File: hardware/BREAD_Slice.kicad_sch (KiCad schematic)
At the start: 0 parts

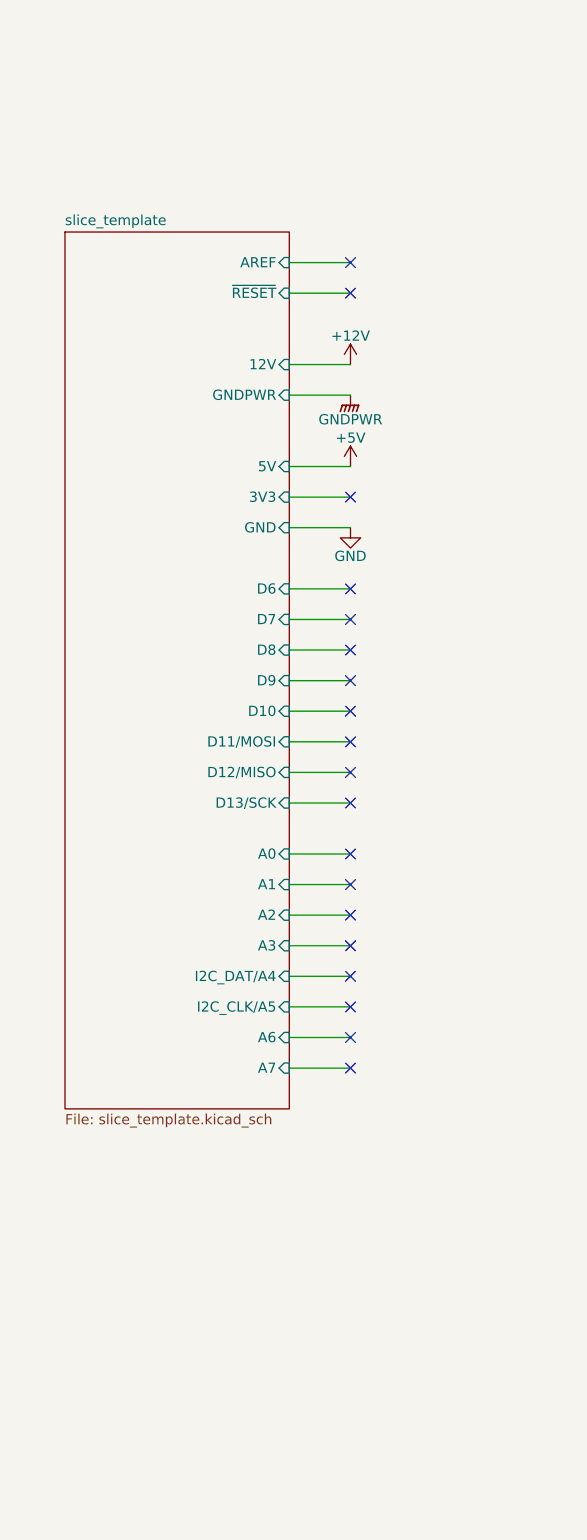
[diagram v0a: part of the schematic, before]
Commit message: Changed to Pico from nano
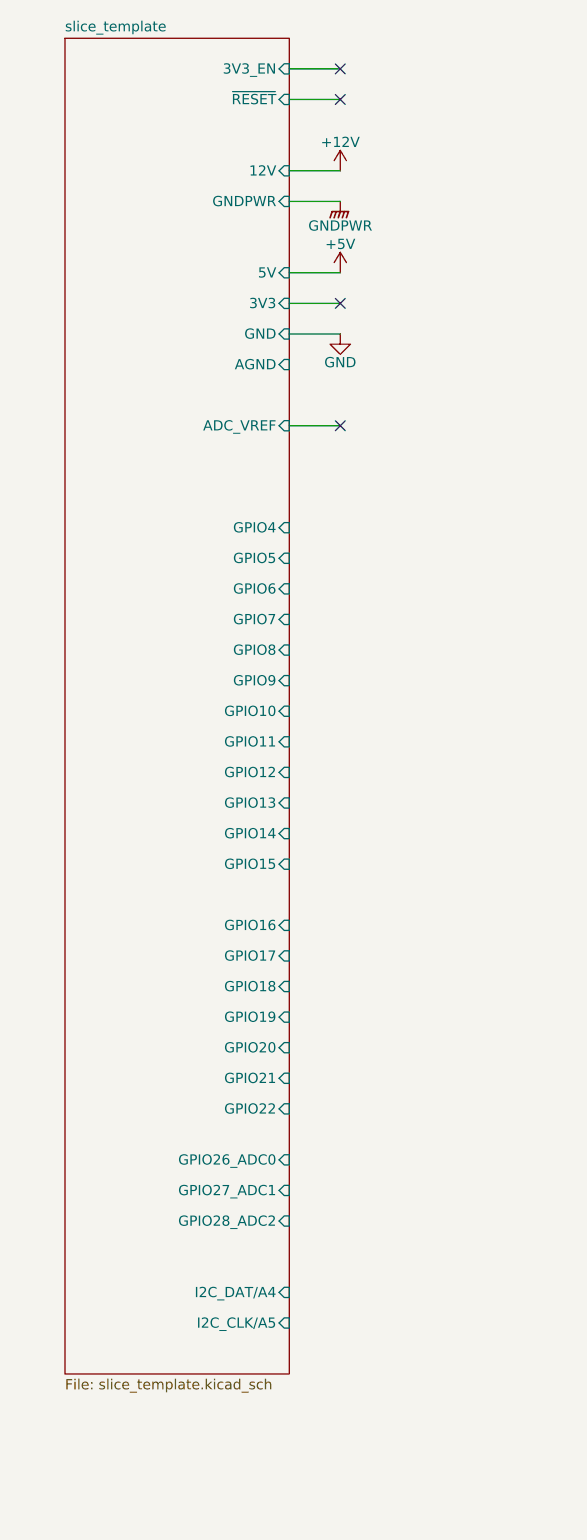
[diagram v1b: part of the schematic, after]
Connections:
- no-connect marks 19 -> 4
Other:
- sheet slice_template ports: added 3V3_EN, ADC_VREF, AGND, GPIO10, GPIO11, GPIO12, GPIO13, GPIO14, GPIO15, GPIO16, GPIO17, GPIO18, GPIO19, GPIO20, GPIO21, GPIO22, GPIO26_ADC0, GPIO27_ADC1, GPIO28_ADC2, GPIO4, GPIO5, GPIO6, GPIO7, GPIO8, GPIO9; removed A0, A1, A2, A3, A6, A7, AREF, D10, D11/MOSI, D12/MISO, D13/SCK, D6, D7, D8, D9

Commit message: added i2c and spi
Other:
- sheet slice_template ports: added I2C_CLK/GPIO7, I2C_SDA/GPIO6, SPI0_MISO/GPIO16, SPI0_MOSI/GPIO19, SPI0_SCK/GPIO18, SPI0_~{CS}/GPIO17; removed GPIO16, GPIO17, GPIO18, GPIO19, GPIO6, GPIO7, I2C_CLK/A5, I2C_DAT/A4
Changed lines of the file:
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@@
-			)
-		)
-		(pin "I2C_CLK{slash}A5" input
-			(at 45.72 177.8 0)
-			(effects
-				(font
-					(size 1.27 1.27)
-				)
-				(justify right)
-			)
-		)
-		(pin "I2C_DAT{slash}A4" input
-			(at 45.72 173.99 0)
-			(effects
-				(font
-					(size 1.27 1.27)
-				)
-				(justify right)
 			)
 		)
@@
 			)
 		)
-		(pin "GPIO6" input
-			(at 45.72 86.36 0)
-			(effects
-				(font
-					(size 1.27 1.27)
-				)
-				(justify right)
-			)
-		)
-		(pin "GPIO7" input
-			(at 45.72 90.17 0)
-			(effects
-				(font
-					(size 1.27 1.27)
-				)
-				(justify right)
-			)
-		)
 		(pin "GPIO8" input
 			(at 45.72 93.98 0)
@@
 			)
 		)
-		(pin "GPIO16" input
-			(at 45.72 128.27 0)
-			(effects
-				(font
-					(size 1.27 1.27)
-				)
-				(justify right)
-			)
-		)
 		(pin "AGND" input
 			(at 45.72 58.42 0)
@@
 			)
 		)
-		(pin "GPIO17" input
-			(at 45.72 132.08 0)
-			(effects
-				(font
-					(size 1.27 1.27)
-				)
-				(justify right)
-			)
-		)
-		(pin "GPIO18" input
-			(at 45.72 135.89 0)
-			(effects
-				(font
-					(size 1.27 1.27)
-				)
-				(justify right)
-			)
-		)
-		(pin "GPIO19" input
-			(at 45.72 139.7 0)
-			(effects
-				(font
-					(size 1.27 1.27)
-				)
-				(justify right)
-			)
-		)
 		(pin "GPIO20" input
-			(at 45.72 143.51 0)
+			(at 45.72 148.59 0)
 			(effects
 				(font
@@
 		)
 		(pin "GPIO21" input
-			(at 45.72 147.32 0)
+			(at 45.72 152.4 0)
 			(effects
 				(font
@@
 		)
 		(pin "GPIO22" input
-			(at 45.72 151.13 0)
+			(at 45.72 156.21 0)
 			(effects
 				(font
@@
 		)
 		(pin "GPIO26_ADC0" input
-			(at 45.72 157.48 0)
+			(at 45.72 168.91 0)
 			(effects
 				(font
@@
 		)
 		(pin "GPIO27_ADC1" input
-			(at 45.72 161.29 0)
+			(at 45.72 172.72 0)
 			(effects
 				(font
@@
 		)
 		(pin "GPIO28_ADC2" input
-			(at 45.72 165.1 0)
-			(effects
-				(font
+			(at 45.72 176.53 0)
+			(effects
+				(font
+					(size 1.27 1.27)
+				)
+				(justify right)
+			)
+		)
+		(pin "I2C_CLK{slash}GPIO7" input
+			(at 45.72 90.17 0)
+			(effects
+				(font
+					(size 1.27 1.27)
+				)
+				(justify right)
+			)
+		)
+		(pin "I2C_SDA{slash}GPIO6" input
+			(at 45.72 86.36 0)
+			(effects
+				(font
+					(size 1.27 1.27)
+				)
+				(justify right)
+			)
+		)
+		(pin "SPI0_MISO{slash}GPIO16" input
+			(at 45.72 133.35 0)
+			(effects
+				(font
+					(size 1.27 1.27)
+				)
+				(justify right)
+			)
+		)
+		(pin "SPI0_MOSI{slash}GPIO19" input
+			(at 45.72 144.78 0)
+			(effects
+				(font
+					(size 1.27 1.27)
+				)
+				(justify right)
+			)
+		)
+		(pin "SPI0_SCK{slash}GPIO18" input
+			(at 45.72 140.97 0)
+			(effects
+				(font
+					(size 1.27 1.27)
+				)
+				(justify right)
+			)
+		)
+		(pin "SPI0_~{CS}{slash}GPIO17" input
+			(at 45.72 137.16 0)
+			(effects
+				(font

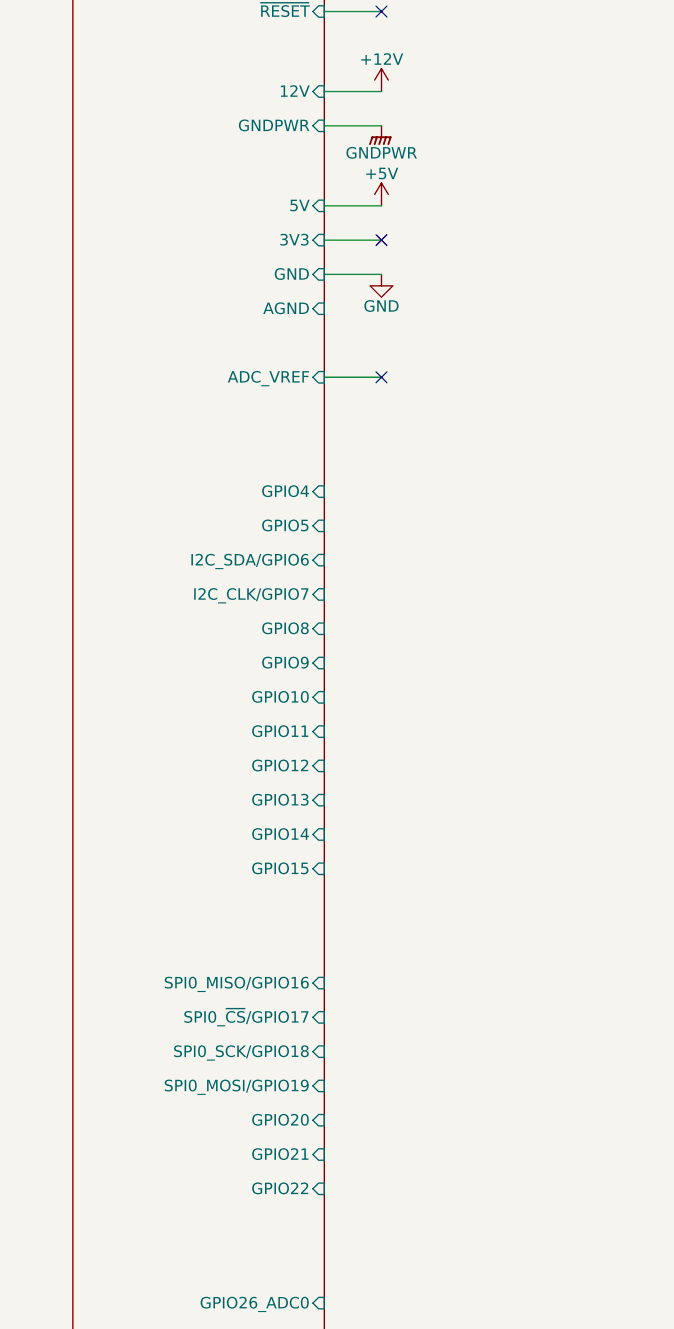
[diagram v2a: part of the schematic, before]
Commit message: added level shifter and started layout
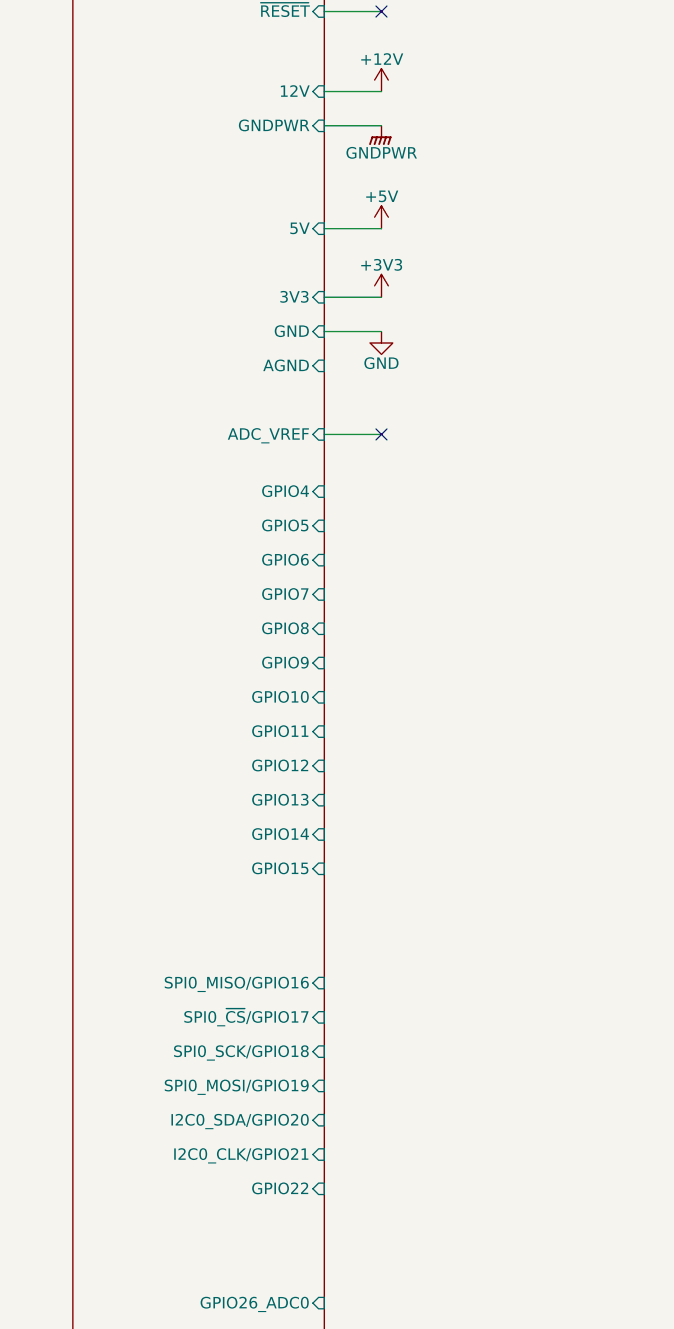
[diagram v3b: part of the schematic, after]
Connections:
- no-connect marks 4 -> 3
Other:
- sheet slice_template ports: added GPIO6, GPIO7, I2C0_CLK/GPIO21, I2C0_SDA/GPIO20; removed GPIO20, GPIO21, I2C_CLK/GPIO7, I2C_SDA/GPIO6
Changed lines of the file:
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@@
 	)
 	(no_connect
-		(at 52.07 50.8)
-	)
-	(no_connect
-		(at 52.07 66.04)
-	)
-	(wire
-		(pts
-			(xy 45.72 54.61) (xy 52.07 54.61)
-		)
-		(stroke
-			(width 0.2032)
-			(type default)
-		)
-	)
-	(wire
-		(pts
-			(xy 45.72 46.99) (xy 52.07 46.99)
+		(at 52.07 72.39)
+	)
+	(wire
+		(pts
+			(xy 45.72 60.96) (xy 52.07 60.96)
+		)
+		(stroke
+			(width 0.2032)
+			(type default)
+		)
+	)
+	(wire
+		(pts
+			(xy 45.72 49.53) (xy 52.07 49.53)
 		)
 		(stroke
@@
 	(wire
 		(pts
-			(xy 45.72 66.04) (xy 52.07 66.04)
-		)
-		(stroke
-			(width 0.2032)
-			(type default)
-		)
-	)
-	(wire
-		(pts
-			(xy 45.72 50.8) (xy 52.07 50.8)
+			(xy 45.72 72.39) (xy 52.07 72.39)
+		)
+		(stroke
+			(width 0.2032)
+			(type default)
+		)
+	)
+	(wire
+		(pts
+			(xy 45.72 57.15) (xy 52.07 57.15)
 		)
 		(stroke
@@
 	(symbol
 		(lib_id "power:+5V")
-		(at 52.07 46.99 0)
+		(at 52.07 49.53 0)
 		(unit 1)
 		(exclude_from_sim no)
@@
 		(dnp no)
 		(property "Reference" "#PWR03"
-			(at 52.07 50.8 0)
+			(at 52.07 53.34 0)
 			(effects
 				(font
@@
 		)
 		(property "Value" "+5V"
-			(at 52.07 43.434 0)
+			(at 52.07 45.974 0)
 			(effects
 				(font
@@
 		)
 		(property "Footprint" ""
-			(at 52.07 46.99 0)
+			(at 52.07 49.53 0)
 			(effects
 				(font
@@
 		)
 		(property "Datasheet" ""
-			(at 52.07 46.99 0)
+			(at 52.07 49.53 0)
 			(effects
 				(font
@@
 		)
 		(property "Description" "Power symbol creates a global label with name \"+5V\""
-			(at 52.07 46.99 0)
+			(at 52.07 49.53 0)
 			(effects
 				(font
@@
 	)
 	(symbol
+		(lib_id "power:+5V")
+		(at 52.07 57.15 0)
+		(unit 1)
+		(exclude_from_sim no)
+		(in_bom yes)
+		(on_board yes)
+		(dnp no)
+		(property "Reference" "#PWR05"
+			(at 52.07 60.96 0)
+			(effects
+				(font
+					(size 1.27 1.27)
+				)
+				(hide yes)
+			)
+		)
+		(property "Value" "+3V3"
+			(at 52.07 53.594 0)
+			(effects
+				(font
+					(size 1.27 1.27)
+				)
+			)
+		)
+		(property "Footprint" ""
+			(at 52.07 57.15 0)
+			(effects
+				(font
+					(size 1.27 1.27)
+				)
+				(hide yes)
+			)
+		)
+		(property "Datasheet" ""
+			(at 52.07 57.15 0)
+			(effects
+				(font
+					(size 1.27 1.27)
+				)
+				(hide yes)
+			)
+		)
+		(property "Description" "Power symbol creates a global label with name \"+5V\""
+			(at 52.07 57.15 0)
+			(effects
+				(font
+					(size 1.27 1.27)
+				)
+				(hide yes)
+			)
+		)
+		(pin "1"
+		)
+		(instances
+			(project "BREAD_Slice"
+				(path "/66043bca-a260-4915-9fce-8a51d324c687"
+					(reference "#PWR05")
+					(unit 1)
+				)
+			)
+		)
+	)
+	(symbol
 		(lib_id "power:GND")
-		(at 52.07 54.61 0)
+		(at 52.07 60.96 0)
 		(unit 1)
 		(exclude_from_sim no)
@@
 		(dnp no)
 		(property "Reference" "#PWR04"
+			(at 52.07 67.31 0)
+			(effects
+				(font
+					(size 1.27 1.27)
+				)
+				(hide yes)
+			)
+		)
+		(property "Value" "GND"
+			(at 52.07 64.516 0)
+			(effects
+				(font
+					(size 1.27 1.27)
+				)
+			)
+		)
+		(property "Footprint" ""
 			(at 52.07 60.96 0)
 			(effects
@@
 			)
 		)
-		(property "Value" "GND"
-			(at 52.07 58.166 0)
-			(effects
-				(font
-					(size 1.27 1.27)
-				)
-			)
-		)
-		(property "Footprint" ""
-			(at 52.07 54.61 0)
-			(effects
-				(font
-					(size 1.27 1.27)
-				)
-				(hide yes)
-			)
-		)
 		(property "Datasheet" ""
-			(at 52.07 54.61 0)
+			(at 52.07 60.96 0)
 			(effects
 				(font
@@
 		)
 		(property "Description" "Power symbol creates a global label with name \"GND\" , ground"
-			(at 52.07 54.61 0)
+			(at 52.07 60.96 0)
 			(effects
 				(font
@@
 		)
 		(pin "3V3" input
-			(at 45.72 50.8 0)
+			(at 45.72 57.15 0)
 			(effects
 				(font
@@
 		)
 		(pin "5V" input
-			(at 45.72 46.99 0)
+			(at 45.72 49.53 0)
 			(effects
 				(font
@@
 		)
 		(pin "GND" input
-			(at 45.72 54.61 0)
+			(at 45.72 60.96 0)
 			(effects
 				(font
@@
 		)
 		(pin "ADC_VREF" input
-			(at 45.72 66.04 0)
+			(at 45.72 72.39 0)
 			(effects
 				(font
@@
 		)
 		(pin "AGND" input
-			(at 45.72 58.42 0)
-			(effects
-				(font
-					(size 1.27 1.27)
-				)
-				(justify right)
-			)
-		)
-		(pin "GPIO20" input
-			(at 45.72 148.59 0)
-			(effects
-				(font
-					(size 1.27 1.27)
-				)
-				(justify right)
-			)
-		)
-		(pin "GPIO21" input
-			(at 45.72 152.4 0)
+			(at 45.72 64.77 0)
 			(effects
 				(font
@@
 			)
 		)
-		(pin "I2C_CLK{slash}GPIO7" input
-			(at 45.72 90.17 0)
-			(effects
-				(font
-					(size 1.27 1.27)
-				)
-				(justify right)
-			)
-		)
-		(pin "I2C_SDA{slash}GPIO6" input
-			(at 45.72 86.36 0)
-			(effects
-				(font
-					(size 1.27 1.27)
-				)
-				(justify right)
-			)
-		)
 		(pin "SPI0_MISO{slash}GPIO16" input
 			(at 45.72 133.35 0)
@@
 			(effects
 				(font
+					(size 1.27 1.27)
+				)
+				(justify right)
+			)
+		)
+		(pin "GPIO6" input
+			(at 45.72 86.36 0)
+			(effects
+				(font
+					(size 1.27 1.27)
+				)
+				(justify right)
+			)
+		)
+		(pin "GPIO7" input
+			(at 45.72 90.17 0)
+			(effects
+				(font
+					(size 1.27 1.27)
+				)
+				(justify right)
+			)
+		)
+		(pin "I2C0_CLK{slash}GPIO21" input
+			(at 45.72 152.4 0)
+			(effects
+				(font
+					(size 1.27 1.27)
+				)
+				(justify right)
+			)
+		)
+		(pin "I2C0_SDA{slash}GPIO20" input
+			(at 45.72 148.59 0)
+			(effects
+				(font

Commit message: finished layout
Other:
- sheet slice_template ports: added GPIO16, GPIO17, GPIO18, GPIO19; removed GPIO22, GPIO26_ADC0, SPI0_MISO/GPIO16, SPI0_MOSI/GPIO19, SPI0_SCK/GPIO18, SPI0_~{CS}/GPIO17
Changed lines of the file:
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@@
-			)
-		)
-		(pin "GPIO22" input
-			(at 45.72 156.21 0)
-			(effects
-				(font
-					(size 1.27 1.27)
-				)
-				(justify right)
-			)
-		)
-		(pin "GPIO26_ADC0" input
-			(at 45.72 168.91 0)
-			(effects
-				(font
-					(size 1.27 1.27)
-				)
-				(justify right)
 			)
 		)
@@
 		(pin "GPIO28_ADC2" input
 			(at 45.72 176.53 0)
-			(effects
-				(font
-					(size 1.27 1.27)
-				)
-				(justify right)
-			)
-		)
-		(pin "SPI0_MISO{slash}GPIO16" input
-			(at 45.72 133.35 0)
-			(effects
-				(font
-					(size 1.27 1.27)
-				)
-				(justify right)
-			)
-		)
-		(pin "SPI0_MOSI{slash}GPIO19" input
-			(at 45.72 144.78 0)
-			(effects
-				(font
-					(size 1.27 1.27)
-				)
-				(justify right)
-			)
-		)
-		(pin "SPI0_SCK{slash}GPIO18" input
-			(at 45.72 140.97 0)
-			(effects
-				(font
-					(size 1.27 1.27)
-				)
-				(justify right)
-			)
-		)
-		(pin "SPI0_~{CS}{slash}GPIO17" input
-			(at 45.72 137.16 0)
 			(effects
 				(font
@@
 			(effects
 				(font
+					(size 1.27 1.27)
+				)
+				(justify right)
+			)
+		)
+		(pin "GPIO16" input
+			(at 45.72 124.46 0)
+			(effects
+				(font
+					(size 1.27 1.27)
+				)
+				(justify right)
+			)
+		)
+		(pin "GPIO17" input
+			(at 45.72 128.27 0)
+			(effects
+				(font
+					(size 1.27 1.27)
+				)
+				(justify right)
+			)
+		)
+		(pin "GPIO18" input
+			(at 45.72 132.08 0)
+			(effects
+				(font
+					(size 1.27 1.27)
+				)
+				(justify right)
+			)
+		)
+		(pin "GPIO19" input
+			(at 45.72 135.89 0)
+			(effects
+				(font
